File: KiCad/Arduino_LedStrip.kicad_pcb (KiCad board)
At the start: 2 copper layers, 48 x 60.5 mm, 30 parts, among them J1 Conn_L, J10 Screw_Terminal_01x01, J2 Conn_R, J3 LED0, J4 LED1, J5 LED_WS2812B, J6 Barrel_Jack, J7 Screw_Terminal_01x01, J8 Screw_Terminal_01x01, J9 Screw_Terminal_01x01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

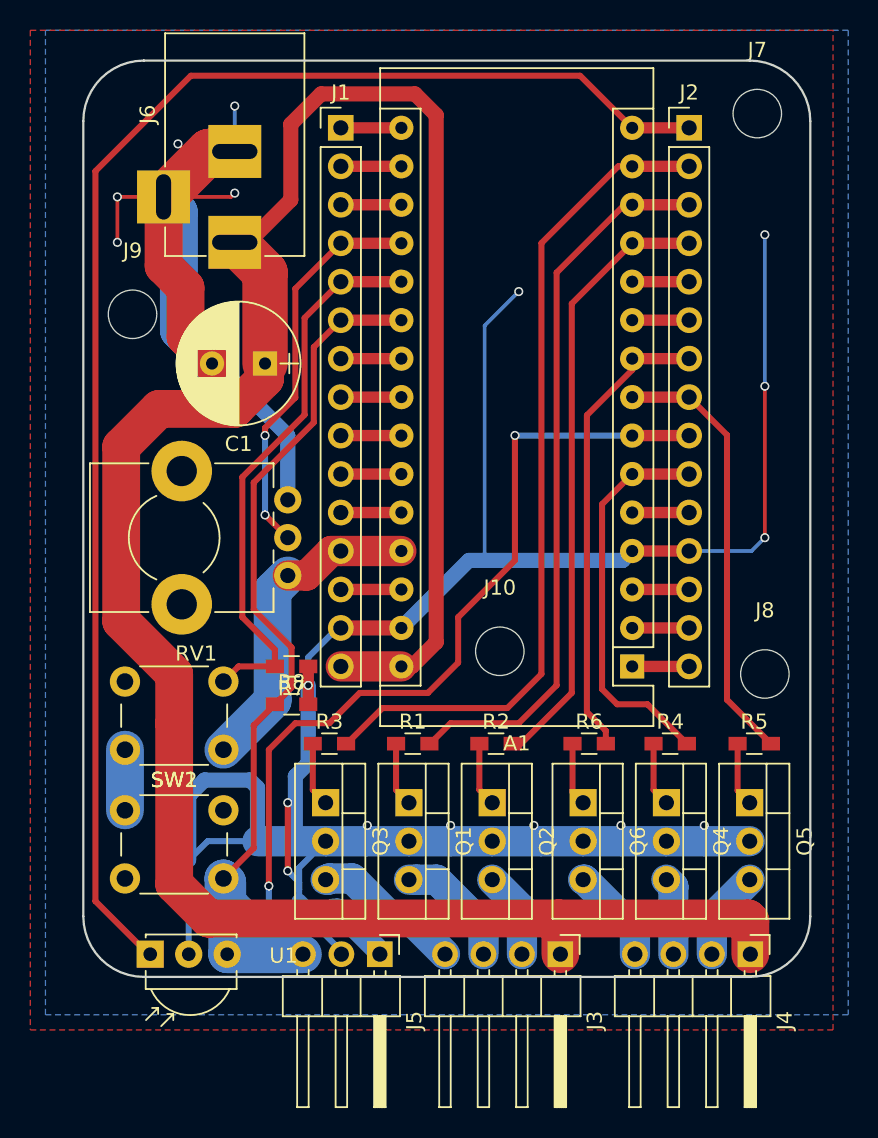
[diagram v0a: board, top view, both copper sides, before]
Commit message: Finish routing. Rearrange folders. Add Arduino folder with sketch.
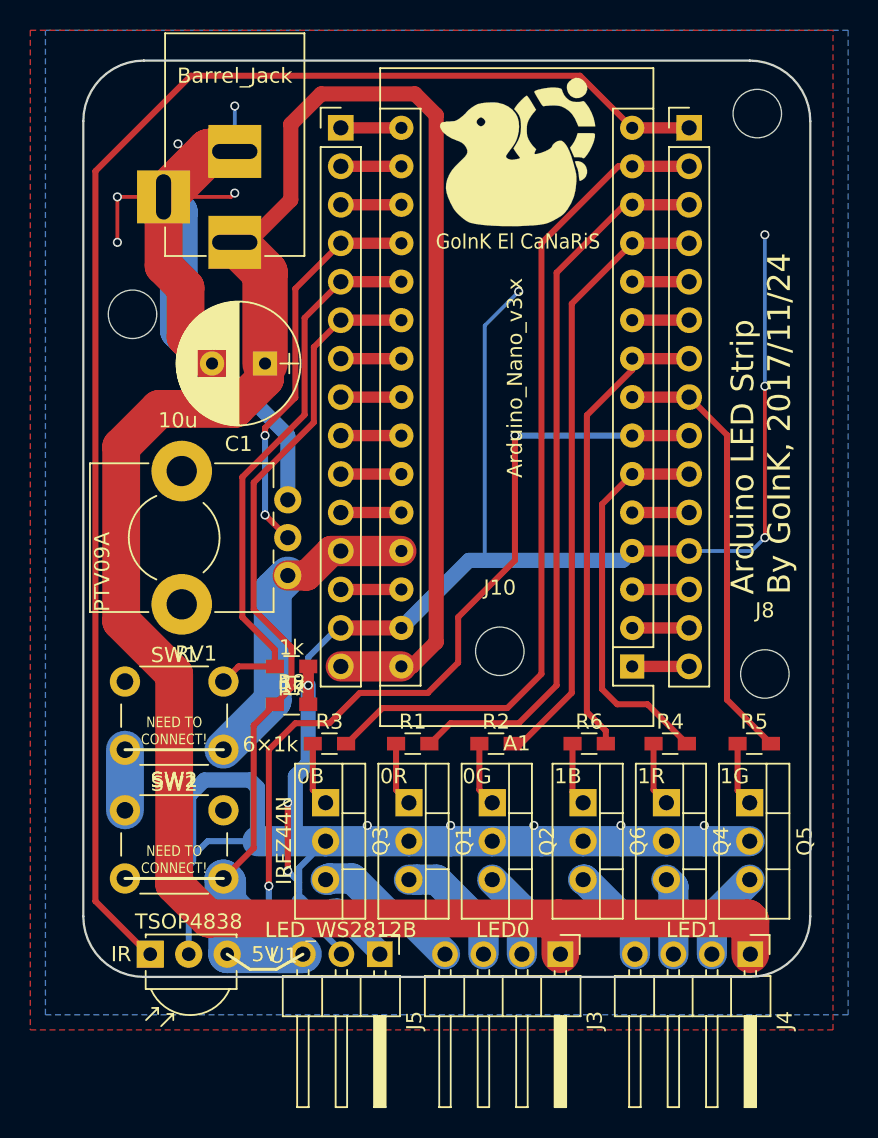
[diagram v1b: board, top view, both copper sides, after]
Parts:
- added G***: LOGO, GoInK13:GoInK600, F.Cu at (151.0, 58.2)
- added G***: LOGO, GoInK13:GoInK300, B.Cu at (144.5, 73.8)
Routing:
- net /ar_A2_D16: track 46.1 -> 55.3 mm
- net +5V: track 43.6 -> 34.4 mm
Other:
- board text added: "0B"
- board text added: "0G"
- board text added: "0R"
- board text added: "12V"
- board text added: "1B"
- board text added: "1G"
- board text added: "1R"
- board text added: "3V3"
- board text added: "5V"
- board text added: "6×1k"
- board text added: "Arduino LED Strip By GoInK, 2017/11/24"
- board text added: "B"
- board text added: "Din"
- board text added: "G"
- board text added: "GND"
- board text added: "GoInK El CaNaRiS"
- board text added: "IR"
- board text added: "LED0"
- board text added: "LED0_B"
- board text added: "LED0_G"
- board text added: "LED0_R"
- board text added: "LED1"
- board text added: "LED1_B"
- board text added: "LED1_R"
- board text added: "LEDWS_Din"
- board text added: "LED_BuiltIn"
- board text added: "NEED TO CONNECT!"
- board text added: "R"

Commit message: Update schematic. Change NMOS_GSD to GDS (TO220). Change 5V IR
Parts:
- moved SW2 7.91 mm to (131.8, 106.0), turned to 180 degrees
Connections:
- Q1 pad 2: GND -> /LED0_R
- Q1 pad 3: /LED0_R -> GND
- Q2 pad 2: GND -> /LED0_G
- Q2 pad 3: /LED0_G -> GND
- Q3 pad 2: GND -> /LED0_B
- Q3 pad 3: /LED0_B -> GND
- Q4 pad 2: GND -> /LED1_R
- Q4 pad 3: /LED1_R -> GND
- Q5 pad 2: GND -> /LED1_G
- Q5 pad 3: /LED1_G -> GND
- Q6 pad 2: GND -> /LED1_B
- Q6 pad 3: /LED1_B -> GND
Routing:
- net GND: track 236.4 -> 328.9 mm, vias 17 -> 30
- net /ar_A2_D16: track 55.3 -> 41.6 mm
- net /LED1_G: track 5.96 -> 12.0 mm
- net /LED1_R: track 5.11 -> 10.2 mm
- net /LED0_G: track 5.73 -> 10.5 mm
- net /LED1_B: track 6.38 -> 9.93 mm
- net +5V: track 34.4 -> 37.2 mm
- net /LED0_R: track 8.03 -> 10.5 mm
- net /LED0_B: track 9.98 -> 11.8 mm
- added copper zone on B.Cu, net +5V
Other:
- board text added: "Arduino LED Strip V1r1 By GoInK, 2017/12/17"
- board text removed: "Arduino LED Strip By GoInK, 2017/11/24"

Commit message: Change mode when simple click during animation. Show old value in mode 4 when in settings.
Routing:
- net +5V: track 37.2 -> 47.0 mm
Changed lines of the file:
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@@
     (links 83)
     (no_connects 3)
-    (area 122.424999 51.924999 170.575001 112.575001)
+    (area 117.111428 40.3 185.85 121.785001)
     (thickness 1.6)
     (drawings 74)
-    (tracks 324)
+    (tracks 328)
     (zones 0)
     (modules 32)
@@
   )
   (setup
-    (last_trace_width 0.4)
+    (last_trace_width 0.25)
     (user_trace_width 0.4)
     (user_trace_width 0.75)
@@
   (segment (start 139.5 81.84) (end 143.5 81.84) (width 0.75) (layer F.Cu) (net 20))
   (segment (start 162.5 66.6) (end 158.74 66.6) (width 0.75) (layer F.Cu) (net 21))
+  (segment (start 131.75 97.5) (end 131.75 98.25) (width 0.25) (layer F.Cu) (net 22))
+  (segment (start 131.75 98.25) (end 130.25 99.75) (width 0.25) (layer F.Cu) (net 22))
+  (segment (start 130.25 99.75) (end 130.25 104.5) (width 0.25) (layer F.Cu) (net 22))
+  (segment (start 130.25 104.5) (end 131.75 106) (width 0.25) (layer F.Cu) (net 22))
   (segment (start 125.25 97.5) (end 128.5 100.75) (width 0.4) (layer B.Cu) (net 22))
   (segment (start 128.5 100.75) (end 128.5 102.75) (width 2.5) (layer B.Cu) (net 22))

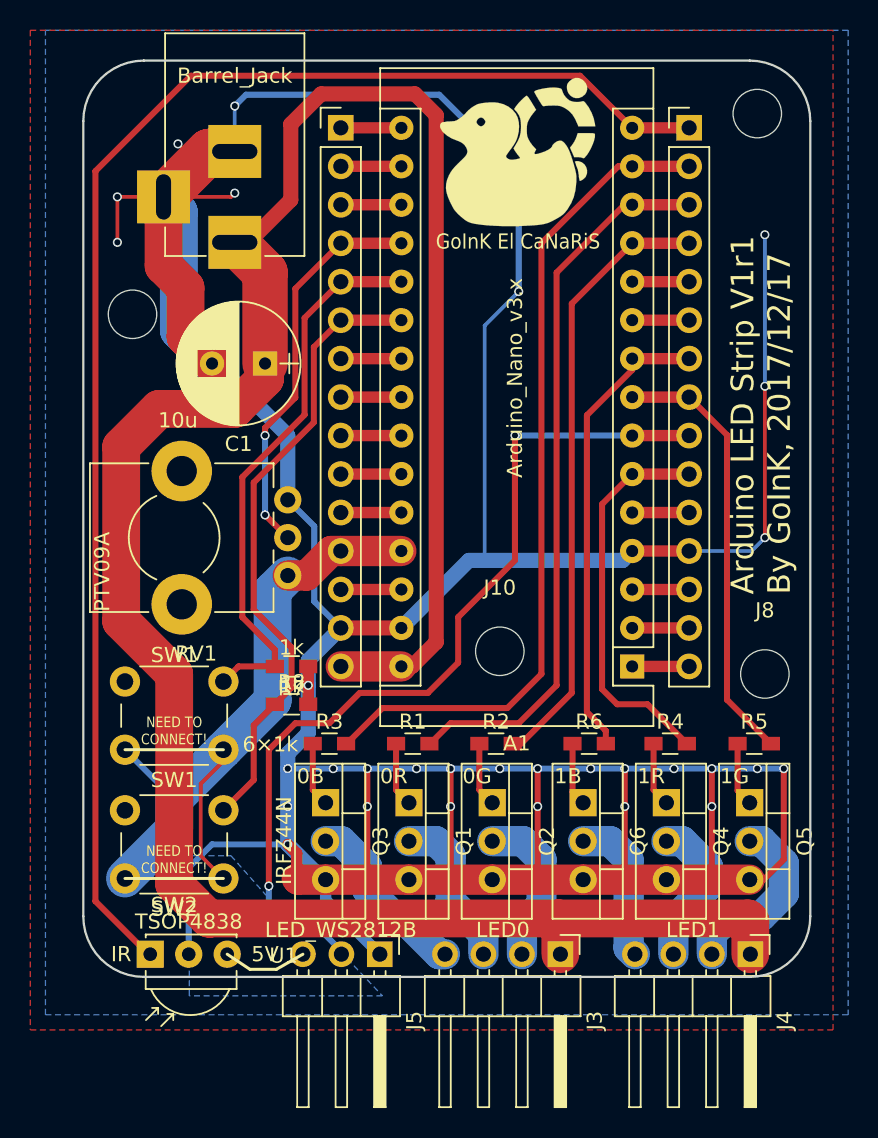
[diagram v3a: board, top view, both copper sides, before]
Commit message: Add possibility to use a 5V or 12V power. Create new gerbers
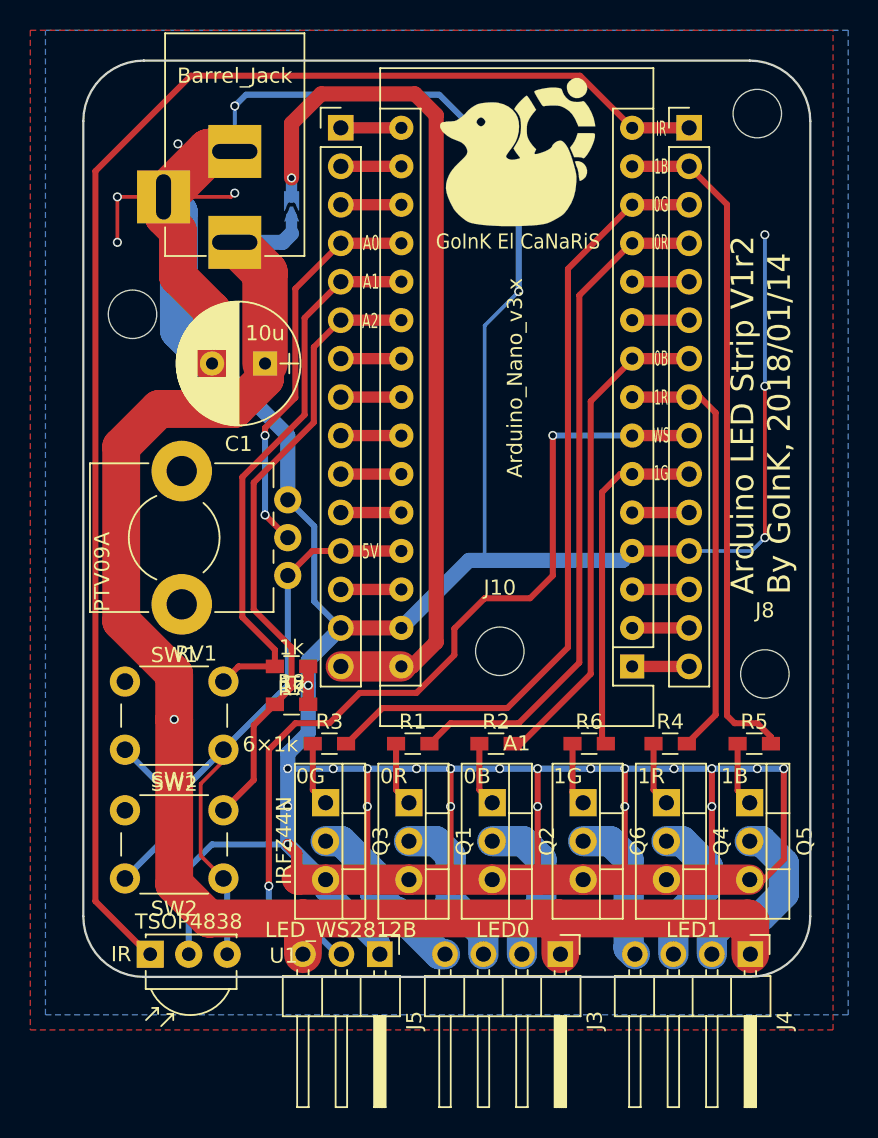
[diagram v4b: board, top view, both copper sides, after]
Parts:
- added R10: 0, Battery_pads:R_Shunt, B.Cu at (136.2, 61.6)
- added R11: 0, Battery_pads:R_Shunt, B.Cu at (128.5, 97.5)
- added REF***: OSHW-Logo_5.7x6mm_SilkScreen, Symbols:OSHW-Logo_5.7x6mm_SilkScreen, B.Cu at (126.8, 55.8)
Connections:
- A1 pad 12: /ar_LED0_G -> /ar_LED0_R
- A1 pad 13: /ar_LED0_R -> /ar_LED0_G
- A1 pad 14: /ar_LED0_B -> /ar_LED1_B
- A1 pad 30: +12V -> /Vin
- A1 pad 6: /ar_LED1_R -> /ar_LED1_G
- A1 pad 8: /ar_LED1_G -> /ar_LED1_R
- A1 pad 9: /ar_LED1_B -> /ar_LED0_B
- J1 pad 15: +12V -> /Vin
- J2 pad 10: /ar_LED1_R -> /ar_LED1_G
- J2 pad 2: /ar_LED0_B -> /ar_LED1_B
- J2 pad 3: /ar_LED0_R -> /ar_LED0_G
- J2 pad 4: /ar_LED0_G -> /ar_LED0_R
- J2 pad 7: /ar_LED1_B -> /ar_LED0_B
- J2 pad 8: /ar_LED1_G -> /ar_LED1_R
- J3 pad 2: /LED0_G -> /LED0_B
- J3 pad 4: /LED0_B -> /LED0_G
- J4 pad 2: /LED1_G -> /LED1_B
- J4 pad 4: /LED1_B -> /LED1_G
- J5 pad 3: +5V -> +12V
- Q2 pad 2: /LED0_G -> /LED0_B
- Q3 pad 2: /LED0_B -> /LED0_G
- Q5 pad 2: /LED1_G -> /LED1_B
- Q6 pad 2: /LED1_B -> /LED1_G
- R2 pad 2: /ar_LED0_G -> /ar_LED0_B
- R3 pad 2: /ar_LED0_B -> /ar_LED0_G
- R5 pad 2: /ar_LED1_G -> /ar_LED1_B
- R6 pad 2: /ar_LED1_B -> /ar_LED1_G
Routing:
- net /Vin: track 0.00 -> 57.6 mm, vias 0 -> 1
- net +12V: track 166.6 -> 113.8 mm, vias 0 -> 1
- net /ar_LED0_B: track 55.1 -> 32.7 mm
- net /ar_LED1_B: track 30.9 -> 45.0 mm
- net /ar_LED0_G: track 40.4 -> 52.1 mm
- net +5V: track 47.0 -> 54.8 mm
- net /ar_LED1_G: track 28.9 -> 23.0 mm
- net /ar_LED0_R: track 47.9 -> 45.1 mm
- net /ar_LED1_R: track 25.9 -> 28.6 mm
- net /LED1_G: track 12.0 -> 9.93 mm
- net /LED1_B: track 9.93 -> 12.0 mm
- net /LED0_B: track 11.8 -> 10.5 mm
- net /LED0_G: track 10.5 -> 11.7 mm
- removed copper zone on B.Cu, net +5V
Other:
- board text added: "/!\ SHUNT if Vin=12V"
- board text added: "/!\ SHUNT if Vin=5V"
- board text added: "A0"
- board text added: "A1"
- board text added: "A2"
- board text added: "Arduino LED Strip V1r2 By GoInK, 2018/01/14"
- board text added: "LED1_G"
- board text added: "Vcc"
- board text added: "WS"
- board text removed: "Arduino LED Strip V1r1 By GoInK, 2017/12/17"
- board text removed: "NEED TO CONNECT!"
